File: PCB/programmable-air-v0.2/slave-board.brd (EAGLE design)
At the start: 101.5 x 50.8 mm, 20 parts, among them Q1 600mA/40V, Q2 600mA/40V, Q3 600mA/40V

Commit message: Post Rube Goldberg. Working on PCB v0.2
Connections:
- net N$15: now also U$9.7
- net VIN: no longer U$9.7
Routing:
- net N$15: track 110.1 -> 165.4 mm, vias 4 -> 5
- net N$13: track 91.1 -> 97.5 mm
- net N$14: track 117.7 -> 122.8 mm
- net VIN: track 228.4 -> 224.3 mm
- net N$12: track 139.6 -> 142.1 mm
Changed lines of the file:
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@@
 <wire x1="73.66" y1="44.093375" x2="73.2282" y2="43.661575" width="0.508" layer="16"/>
 <wire x1="73.2282" y1="43.661575" x2="73.2282" y2="39.9350875" width="0.508" layer="16"/>
+<wire x1="19.05" y1="41.91" x2="19.05" y2="44.45" width="0.508" layer="1"/>
 </signal>
 <signal name="N$13">
@@
 <wire x1="16.51" y1="41.91" x2="16.51" y2="45.72" width="0.508" layer="16"/>
 <via x="16.51" y="45.72" extent="1-16" drill="1.27"/>
-<wire x1="16.51" y1="45.72" x2="17.5795" y2="46.7895" width="0.508" layer="1"/>
+<wire x1="17.5795" y1="46.7895" x2="16.51" y2="45.72" width="0.508" layer="1"/>
 <wire x1="74.37048125" y1="46.7895" x2="75.06898125" y2="46.091" width="0.508" layer="1"/>
 <wire x1="75.06898125" y1="46.091" x2="78.00784375" y2="46.091" width="0.508" layer="1"/>
@@
 <via x="60.96" y="35.56" extent="1-16" drill="1.27"/>
 <wire x1="60.96" y1="35.56" x2="60.96" y2="46.7895" width="0.6096" layer="1"/>
+<wire x1="63.5" y1="35.56" x2="60.96" y2="35.56" width="0.508" layer="1"/>
+<wire x1="16.51" y1="45.72" x2="16.51" y2="41.91" width="0.508" layer="1"/>
 </signal>
 <signal name="N$14">
@@
 <wire x1="13.97" y1="41.91" x2="13.97" y2="46.99" width="0.508" layer="16"/>
 <via x="13.97" y="46.99" extent="1-16" drill="1.27"/>
-<wire x1="14.7855" y1="47.8055" x2="13.97" y2="46.99" width="0.508" layer="1"/>
+<wire x1="13.97" y1="46.99" x2="14.7855" y2="47.8055" width="0.508" layer="1"/>
 <wire x1="77.587" y1="47.107" x2="75.489825" y2="47.107" width="0.508" layer="1"/>
 <wire x1="77.587" y1="47.107" x2="78.74" y2="48.26" width="0.508" layer="1"/>
@@
 <wire x1="74.016625" y1="44.45" x2="74.461125" y2="44.8945" width="0.508" layer="1"/>
 <wire x1="74.461125" y1="44.8945" x2="78.180175" y2="44.8945" width="0.508" layer="1"/>
+<wire x1="13.97" y1="41.91" x2="13.97" y2="46.99" width="0.508" layer="1"/>
 </signal>
 <signal name="N$15">
@@
 <wire x1="12.7" y1="49.52" x2="76.2" y2="49.52" width="0.508" layer="1"/>
 <wire x1="76.2" y1="49.52" x2="76.2" y2="48.8215" width="0.508" layer="1"/>
-<wire x1="66.04" y1="33.02" x2="77.47" y2="33.02" width="0.508" layer="1"/>
+<wire x1="77.47" y1="33.02" x2="66.04" y2="33.02" width="0.508" layer="1"/>
 <wire x1="77.47" y1="33.02" x2="77.47" y2="40.64" width="0.508" layer="1"/>
 <wire x1="77.47" y1="40.64" x2="77.47" y2="40.005" width="0.6096" layer="16"/>
@@
 <wire x1="77.47" y1="40.64" x2="77.47" y2="43.18" width="0.6096" layer="16"/>
 <wire x1="77.47" y1="43.18" x2="77.47" y2="40.64" width="0.6096" layer="1"/>
+<contactref element="U$9" pad="7"/>
+<wire x1="11.43" y1="22.86" x2="11.43" y2="41.91" width="0.508" layer="1"/>
+<wire x1="11.43" y1="22.86" x2="12.7" y2="21.59" width="0.508" layer="1"/>
+<wire x1="12.7" y1="21.59" x2="25.4" y2="21.59" width="0.508" layer="1"/>
+<wire x1="25.4" y1="21.59" x2="30.48" y2="16.51" width="0.508" layer="1"/>
+<via x="33.02" y="16.51" extent="1-16" drill="1"/>
+<wire x1="33.02" y1="16.51" x2="30.48" y2="16.51" width="0.508" layer="16"/>
+<wire x1="30.48" y1="16.51" x2="33.02" y2="16.51" width="0.508" layer="1"/>
+<wire x1="11.43" y1="41.91" x2="11.43" y2="48.8215" width="0.508" layer="1"/>
+<wire x1="66.04" y1="33.02" x2="63.5" y2="33.02" width="0.508" layer="1"/>
 </signal>
 <signal name="VIN">
@@
 <wire x1="78.74" y1="13.97" x2="78.74" y2="3.81" width="2.54" layer="16"/>
 <wire x1="92.71" y1="40.64" x2="97.79" y2="40.64" width="1.27" layer="16"/>
-<contactref element="U$9" pad="7"/>
-<wire x1="30.48" y1="16.51" x2="26.416" y2="16.51" width="0.508" layer="16"/>
 </signal>
 <signal name="GND">
@@
 <wire x1="39.37" y1="21.59" x2="41.91" y2="24.13" width="0.508" layer="16"/>
 <wire x1="41.91" y1="24.13" x2="41.91" y2="25.4" width="0.508" layer="16"/>
-<wire x1="93.98" y1="26.67" x2="84.35" y2="33.22" width="0" layer="19" extent="1-1"/>
-<wire x1="75.05065" y1="40.76065" x2="84.35" y2="33.22" width="0" layer="19" extent="1-16"/>
-<wire x1="63.5" y1="40.64" x2="74.93" y2="40.64" width="0" layer="19" extent="16-16"/>
-<wire x1="64.77" y1="22.86" x2="63.5" y2="40.64" width="0" layer="19" extent="1-1"/>
-<wire x1="41.91" y1="24.13" x2="54.29" y2="18.78" width="0" layer="19" extent="16-16"/>
-<wire x1="19.05" y1="21.59" x2="38.1" y2="21.59" width="0" layer="19" extent="16-16"/>
-<wire x1="17.25" y1="32.82" x2="19.05" y2="27.94" width="0" layer="19" extent="1-1"/>
-<wire x1="8.89" y1="39.37" x2="17.25" y2="32.82" width="0" layer="19" extent="1-1"/>
 </signal>
 <signal name="N$16">

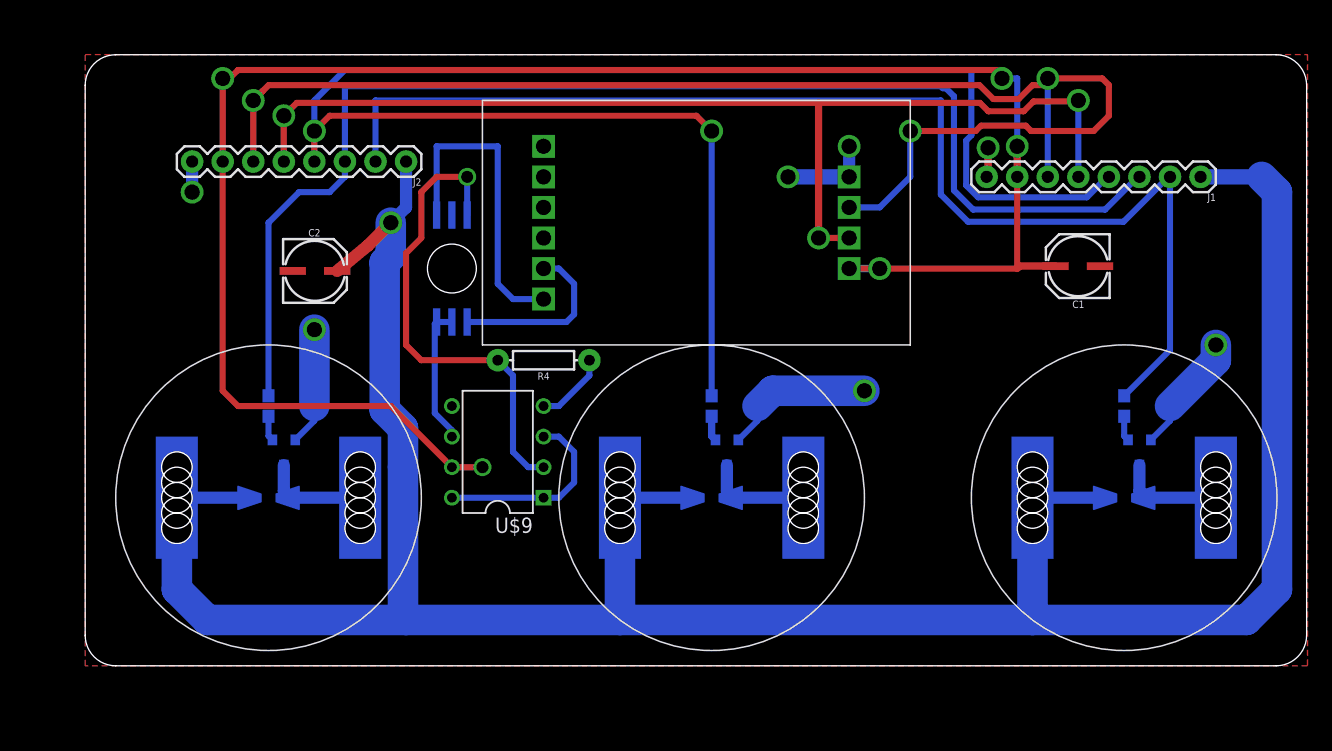
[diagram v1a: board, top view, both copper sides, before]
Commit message: PCB v0.2 slave board ready
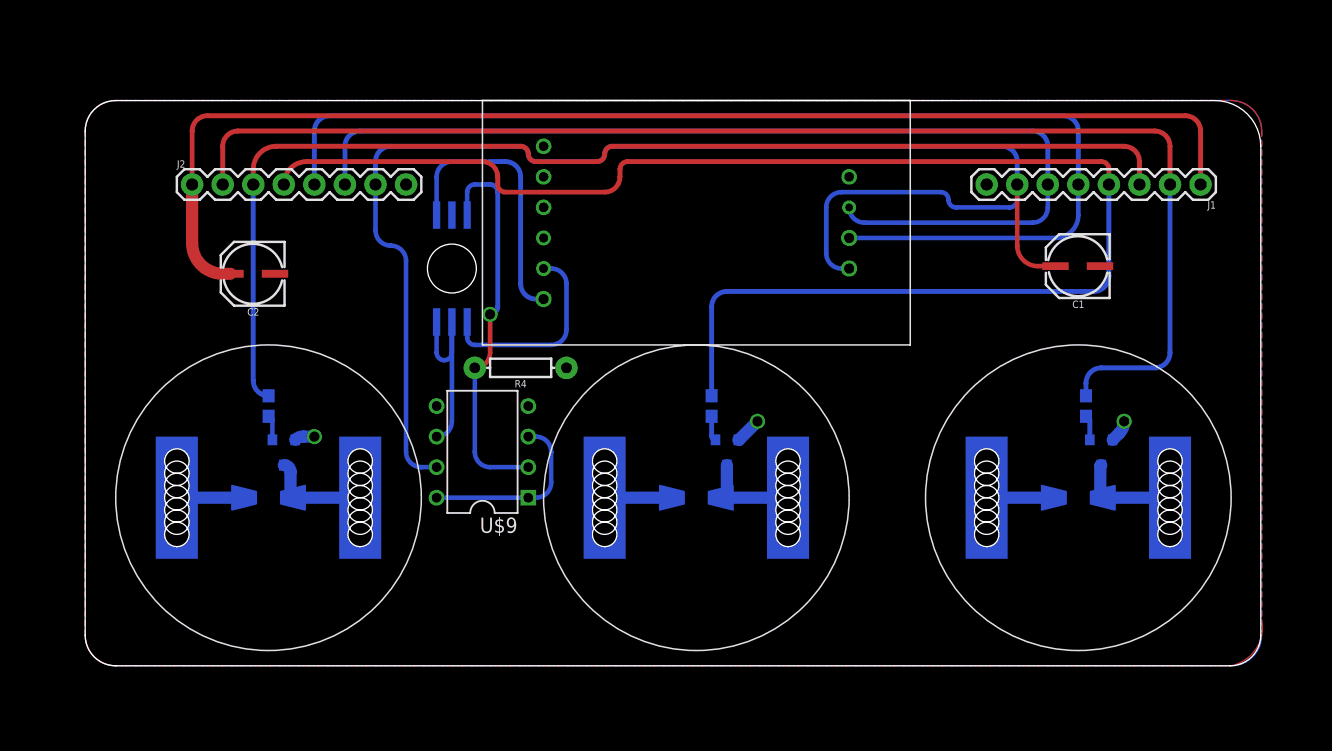
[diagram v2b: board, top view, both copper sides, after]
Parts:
- moved J2 17.9 mm to (8.89, 40.0), turned to 0 degrees
- moved C2 5.12 mm to (14.0, 32.4), turned to 180 degrees
- moved U$4 3.81 mm to (82.5, 14.0)
- moved U$7 3.81 mm to (82.5, 14.0)
- moved Q3 3.17 mm to (84.5, 17.8)
- moved R3 3.17 mm to (83.2, 21.6)
- moved R4 2.01 mm to (36.2, 24.8)
- moved U$2 1.27 mm to (50.8, 14.0)
- moved U$5 1.27 mm to (50.8, 14.0)
- moved U$9 1.27 mm to (33.0, 17.8)
- moved J1 0.63 mm to (92.7, 40.0)
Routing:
- net VIN: track 224.3 -> 120.2 mm, vias 1 -> 0
- net GND: track 54.1 -> 5.71 mm, vias 7 -> 3
- net N$15: track 165.4 -> 119.3 mm, vias 5 -> 0
- net N$14: track 122.8 -> 85.3 mm, vias 3 -> 0
- net N$12: track 142.1 -> 122.8 mm, vias 2 -> 0
- net N$10: track 106.1 -> 97.3 mm
- net N$5: track 101.3 -> 109.2 mm
- net N$17: track 40.1 -> 32.3 mm
- net N$16: track 11.4 -> 16.9 mm
- net N$21: track 26.6 -> 22.5 mm
- net N$22: track 14.8 -> 16.6 mm
- net N$13: track 97.5 -> 95.8 mm, vias 3 -> 0
- net N$4: track 16.3 -> 15.0 mm
- added copper zone on layer 16, net VIN
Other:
- board size 101.5 x 50.8 mm -> 97.7 x 47 mm

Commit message: Minor fixes to slave PCB after assembly. Started work on test code for PCB v0.2
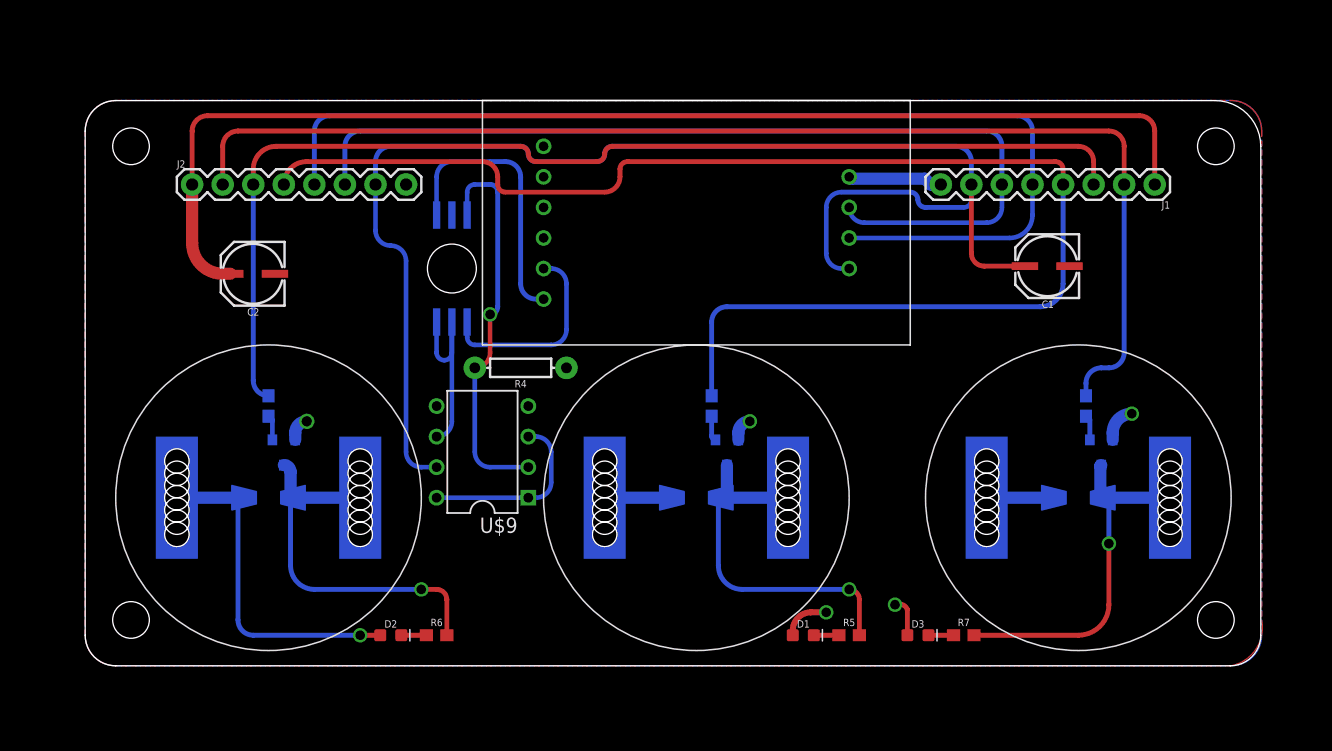
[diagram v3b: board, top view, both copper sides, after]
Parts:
- added D1, D2, D3: GREEN, SparkFun-LED:LED-0603
- added R5, R6, R7: 10k, SparkFun-Resistors:0603
- moved J1 3.81 mm to (88.9, 40.0)
- moved C1 2.54 mm to (80.0, 33.0)
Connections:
- new net N$11: D2.C, R6.1
- new net N$18: D1.C, R5.1
- new net N$6: D3.C, R7.1
- net N$7: now also R7.2
- net N$8: now also R6.2
- net N$9: now also R5.2
- net VIN: now also D1.A, D2.A, D3.A
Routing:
- net VIN: track 120.2 -> 146.3 mm, vias 0 -> 3
- net N$8: track 8.73 -> 31.5 mm, vias 0 -> 1
- net N$9: track 9.14 -> 30.6 mm, vias 0 -> 1
- net N$7: track 8.53 -> 29.7 mm, vias 0 -> 1
- net GND: track 5.71 -> 14.6 mm
- net N$12: track 122.8 -> 114.9 mm
- net N$13: track 95.8 -> 88.2 mm
- net N$5: track 109.2 -> 101.6 mm
- net N$14: track 85.3 -> 77.7 mm
- net N$15: track 119.3 -> 113.3 mm
- net N$10: track 97.3 -> 93.5 mm
- net N$6: track 0.00 -> 2.08 mm
- net N$18: track 0.00 -> 2.08 mm
- net N$11: track 0.00 -> 2.08 mm

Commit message: LM358 slave board ready
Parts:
- removed R4: (no value), SparkFun-Resistors:AXIAL-0.3
- added IC1: INA126U, INA126:SO08
- added IC3: LM358MX, linear:SO08
- added R10: 1.78K, eagle-ltspice:R0603
- added R13, R14, R15, R8, R9: 10K, eagle-ltspice:R0603
- added R16: 40K, eagle-ltspice:R0603
- added R17, R20: 20K, eagle-ltspice:R0603
- added U$10: BUTTON, programmable-air-components:BUTTON
- U$1: value HX711 -> 2SMPP-03; device programmable-air-components:HX711 -> programmable-air-components:2SMPP-03
- U$8: value 2SMPP-03 -> BUTTON; device programmable-air-components:2SMPP-03 -> programmable-air-components:BUTTON
- U$9: value LM10CN -> BUTTON; device programmable-air-components:DIP8 -> programmable-air-components:BUTTON
- moved U$8 34.7 mm to (50.1, 4.46), turned to 180 degrees
- moved U$9 21.2 mm to (16.5, 4.47), turned to 180 degrees
- moved D3 18.5 mm to (87.6, 4.45), turned to 90 degrees
- moved R7 17.8 mm to (87.6, 12.7), flipped to the bottom, turned to 90 degrees
- moved R5 12.9 mm to (56.5, 13.3), flipped to the bottom, turned to 90 degrees
- moved R6 11.4 mm to (22.9, 12.1), flipped to the bottom, turned to 90 degrees
- moved Q2 7.62 mm to (16.5, 25.4), turned to 90 degrees
- moved Q1 7.43 mm to (50.8, 24.8), turned to 90 degrees
- moved Q3 7.43 mm to (81.9, 24.8), turned to 90 degrees
- moved U$3 7.10 mm to (16.5, 21.0)
- moved U$6 7.10 mm to (16.5, 21.0)
- moved U$4 7.10 mm to (81.3, 21.0)
- moved U$7 7.10 mm to (81.3, 21.0)
- moved U$2 7.01 mm to (50.2, 21.0)
- moved U$5 7.01 mm to (50.2, 21.0)
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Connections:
- removed net N$16: U$8.P$5, U$8.P$6, U$9.6
- removed net N$17: R4.P$2, U$8.P$3, U$9.2
- removed net N$21: U$1.P$6, U$8.P$1
- removed net N$22: U$1.P$5, U$8.P$4
- new net N$19: IC3.1, U$1.P$5, U$1.P$6
- new net N$20: IC1.3, U$1.P$4
- new net N$24: IC3.3, R16.1, R8.2
- new net N$25: IC1.8, R10.1
- new net N$26: IC1.1, R10.2
- new net N$27: IC3.6, R13.2, R17.2, R20.1
- new net N$30: IC3.5, R14.2, R15.1
- new net N$31: IC3.2, R9.2, U$1.P$3
- net GND: now also IC1.4, IC3.4, R14.1, R17.1, R8.1, R9.1; no longer R4.P$1, U$1.P$7, U$9.4
- net N$1: now also U$8.P$2, U$8.P$4
- net N$13: now also IC3.7, R13.1; no longer U$1.P$9
- net N$14: no longer U$1.P$8
- net N$15: now also IC1.5, IC3.8, R15.2, R16.2, R20.2, U$10.P$1, U$10.P$3, U$8.P$1, U$8.P$3, U$9.P$1, U$9.P$3; no longer U$1.P$10, U$9.7
- net N$2: now also U$9.P$2, U$9.P$4
- net N$3: now also U$10.P$2, U$10.P$4
- net N$4: now also IC1.2, U$1.P$1; no longer U$9.1, U$9.3, U$9.8
- net VIN: now also IC1.7
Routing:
- net VIN: track 146.3 -> 417.3 mm
- net N$15: track 113.3 -> 322.2 mm, vias 0 -> 2
- net N$14: track 77.7 -> 0.00 mm
- net N$2: track 2.09 -> 39.9 mm, vias 0 -> 1
- net GND: track 14.6 -> 51.6 mm, vias 3 -> 4
- net N$19: track 0.00 -> 35.5 mm, vias 0 -> 2
- net N$3: track 2.09 -> 37.3 mm, vias 0 -> 1
- net N$1: track 2.09 -> 37.2 mm, vias 0 -> 1
- net N$17: track 32.3 -> 0.00 mm, vias 1 -> 0
- net N$21: track 22.5 -> 0.00 mm
- net N$31: track 0.00 -> 17.0 mm
- net N$16: track 16.9 -> 0.00 mm
- net N$22: track 16.6 -> 0.00 mm
- net N$8: track 31.5 -> 15.4 mm, vias 1 -> 0
- net N$27: track 0.00 -> 11.9 mm
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- added copper zone on layer 16, net GND
- removed copper zone on layer 16, net VIN
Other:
- board size 97.7 x 47 mm -> 97.7 x 49 mm

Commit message: Sent for second production run. New Logo.
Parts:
- removed R13, R14, R15: 10K, eagle-ltspice:R0603
- removed R16: 40K, eagle-ltspice:R0603
- removed R17, R20: 20K, eagle-ltspice:R0603
- added C3, C4: 1.0uF, SparkFun-Capacitors:0603
- added C5: 22uF, SparkFun-Capacitors:PANASONIC_C
- added R11, R12, R18, R19, R4: 10k, SparkFun-Resistors:0603
- added R21: 40K, SparkFun-Resistors:0603
- added R22, R23: 20K, SparkFun-Resistors:0603
- added R24: 2K, SparkFun-Resistors:0603
- R10: value 1.78K -> 1k; device eagle-ltspice:R0603 -> SparkFun-Resistors:0603
- R8, R9: value 10K -> 1k; device eagle-ltspice:R0603 -> SparkFun-Resistors:0603
- moved R9 45.1 mm to (23.5, 1.91), flipped to the top, turned to 180 degrees
- moved R10 38.7 mm to (88.3, 1.91), flipped to the top, turned to 180 degrees
- moved R8 35.2 mm to (55.9, 1.91), flipped to the top, turned to 180 degrees
- moved C1 7.67 mm to (71.1, 37.5), turned to 0 degrees
- moved C2 7.18 mm to (8.89, 37.5), turned to 90 degrees
- moved D2 2.29 mm to (24.8, 5.71)
- moved R6 1.91 mm to (24.8, 12.1)
- moved Q1 1.90 mm to (48.9, 24.8)
- moved D3 1.80 mm to (88.9, 5.71)
- moved D1 1.42 mm to (57.1, 5.71)
- moved R7 1.27 mm to (88.9, 12.7)
- moved R1 1.27 mm to (45.7, 24.8)
- moved U$2 1.27 mm to (48.9, 21.0)
- moved U$5 1.27 mm to (48.9, 21.0)
- moved U$8 1.27 mm to (48.9, 4.46)
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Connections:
- removed net N$15: C1.+, IC1.5, IC3.8, J1.7, J2.7, R15.2, R16.2, R20.2, U$10.P$1, U$10.P$3, U$8.P$1, U$8.P$3, U$9.P$1, U$9.P$3
- removed net VIN: C2.+, D1.A, D2.A, D3.A, IC1.7, J1.1, J2.1, U$2.P$1, U$3.P$1, U$4.P$1, U$5.P$1, U$6.P$1, U$7.P$1
- new net N$16: IC1.6, R22.1
- new net N$17: C2.+, C4.1, C5.+, D1.A, D2.A, D3.A, IC1.7, J1.1, J2.1, U$2.P$1, U$3.P$1, U$4.P$1, U$5.P$1, U$6.P$1, U$7.P$1
- new net N$21: R8.2, U$8.P$1, U$8.P$3
- new net N$22: R9.2, U$9.P$1, U$9.P$3
- new net N$23: R10.2, U$10.P$1, U$10.P$3
- new net N$28: C1.+, C3.1, IC1.5, IC3.8, J1.7, J2.7, R10.1, R18.2, R21.1, R8.1, R9.1
- net GND: now also C3.2, C4.2, C5.-, R11.1, R12.1, R23.1, R4.1; no longer R14.1, R17.1, R8.1, R9.1
- net N$13: now also R19.1; no longer R13.1
- net N$24: now also R21.2, R4.2; no longer R16.1, R8.2
- net N$25: now also R24.1; no longer R10.1
- net N$26: now also R24.2; no longer R10.2
- net N$27: now also R19.2, R22.2, R23.2; no longer R13.2, R17.2, R20.1
- net N$30: now also R12.2, R18.1; no longer R14.2, R15.1
- net N$31: now also R11.2; no longer R9.2
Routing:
- net VIN: track 417.3 -> 0.00 mm, vias 3 -> 0
- net N$17: track 0.00 -> 324.4 mm, vias 0 -> 4
- net N$15: track 322.2 -> 0.00 mm, vias 2 -> 0
- net N$28: track 0.00 -> 185.9 mm, vias 0 -> 2
- net N$16: track 0.00 -> 37.7 mm
- net GND: track 51.6 -> 62.7 mm, vias 4 -> 2
- net N$8: track 15.4 -> 25.9 mm
- net N$23: track 0.00 -> 10.3 mm
- net N$22: track 0.00 -> 10.3 mm
- net N$21: track 0.00 -> 10.3 mm
- net N$9: track 22.4 -> 31.5 mm
- net N$24: track 1.99 -> 9.25 mm
- net N$7: track 20.1 -> 25.4 mm
- net N$13: track 97.5 -> 94.4 mm
- net N$31: track 17.0 -> 14.5 mm
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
